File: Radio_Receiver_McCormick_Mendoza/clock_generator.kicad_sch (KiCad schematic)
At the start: 32 parts, among them J10 CLK_2, J11 I_LO, J12 Q_LO, J24 CLK_0, J9 CLK_1, U5 Si5351A-B-GT, U6 SN74AC74DR, Y1 ASTX-H11-24.576MHZ-T

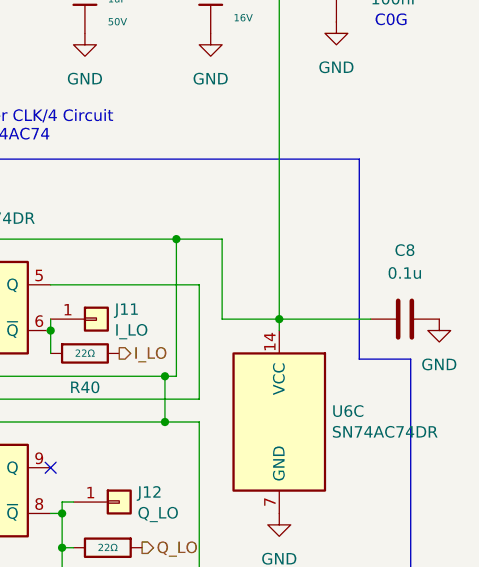
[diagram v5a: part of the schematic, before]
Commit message: Created low mono, high stereo impedance DAC audio outlets
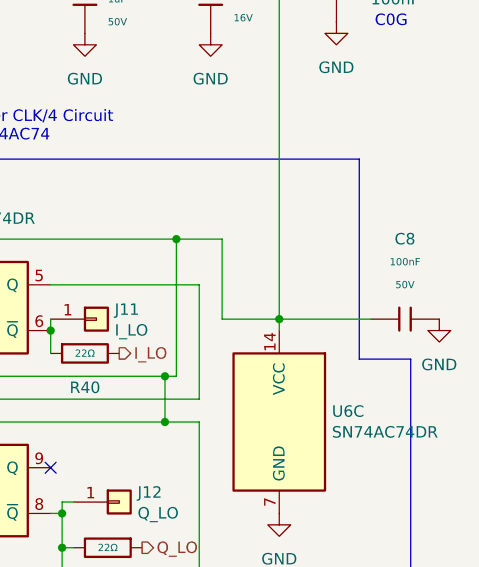
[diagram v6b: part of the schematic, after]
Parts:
- removed C8: 0.1u, Capacitor_THT:C_Disc_D5.1mm_W3.2mm_P5.00mm, symbol Device:C
- added C8: 100nF, PCM_JLCPCB:C_0402, symbol PCM_JLCPCB-Capacitors:0402,100nF,(2)
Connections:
- net GND: now also C8.2
- net at C71.1, C72.1, FB13.2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: now also C8.1
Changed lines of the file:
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@@
+	)
+	(symbol
+		(lib_id "PCM_JLCPCB-Capacitors:0402,100nF,(2)")
+		(at 207.01 82.55 90)
+		(unit 1)
+		(body_style 1)
+		(exclude_from_sim no)
+		(in_bom yes)
+		(on_board yes)
+		(in_pos_files yes)
+		(dnp no)
+		(fields_autoplaced yes)
+		(property "Reference" "C8"
+			(at 207.01 73.66 90)
+			(show_name no)
+			(do_not_autoplace no)
+			(effects
+				(font
+					(size 1.27 1.27)
+				)
+			)
+		)
+		(property "Value" "100nF"
+			(at 207.01 76.2 90)
+			(show_name no)
+			(do_not_autoplace no)
+			(effects
+				(font
+					(size 0.8 0.8)
+				)
+			)
+		)
+		(property "Footprint" "PCM_JLCPCB:C_0402"
+			(at 207.01 84.328 90)
+			(hide yes)
+			(show_name no)
+			(do_not_autoplace no)
+			(effects
+				(font
+					(size 1.27 1.27)
+				)
+			)
+		)
+		(property "Datasheet" "https://www.lcsc.com/datasheet/lcsc_datasheet_2304140030_Samsung-Electro-Mechanics-CL05B104KB54PNC_C307331.pdf"
+			(at 207.01 82.55 0)
+			(hide yes)
+			(show_name no)
+			(do_not_autoplace no)
+			(effects
+				(font
+					(size 1.27 1.27)
+				)
+			)
+		)
+		(property "Description" "50V 100nF X7R ±10% 0402 Multilayer Ceramic Capacitors MLCC - SMD/SMT ROHS"
+			(at 207.01 82.55 0)
+			(hide yes)
+			(show_name no)
+			(do_not_autoplace no)
+			(effects
+				(font
+					(size 1.27 1.27)
+				)
+			)
+		)
+		(property "LCSC" "C307331"
+			(at 207.01 82.55 0)
+			(hide yes)
+			(show_name no)
+			(do_not_autoplace no)
+			(effects
+				(font
+					(size 1.27 1.27)
+				)
+			)
+		)
+		(property "Stock" "8389599"
+			(at 207.01 82.55 0)
+			(hide yes)
+			(show_name no)
+			(do_not_autoplace no)
+			(effects
+				(font
+					(size 1.27 1.27)
+				)
+			)
+		)
+		(property "Price" "0.008USD"
+			(at 207.01 82.55 0)
+			(hide yes)
+			(show_name no)
+			(do_not_autoplace no)
+			(effects
+				(font
+					(size 1.27 1.27)
+				)
+			)
+		)
+		(property "Process" "SMT"
+			(at 207.01 82.55 0)
+			(hide yes)
+			(show_name no)
+			(do_not_autoplace no)
+			(effects
+				(font
+					(size 1.27 1.27)
+				)
+			)
+		)
+		(property "Minimum Qty" "20"
+			(at 207.01 82.55 0)
+			(hide yes)
+			(show_name no)
+			(do_not_autoplace no)
+			(effects
+				(font
+					(size 1.27 1.27)
+				)
+			)
+		)
+		(property "Attrition Qty" "10"
+			(at 207.01 82.55 0)
+			(hide yes)
+			(show_name no)
+			(do_not_autoplace no)
+			(effects
+				(font
+					(size 1.27 1.27)
+				)
+			)
+		)
+		(property "Class" "Basic Component"
+			(at 207.01 82.55 0)
+			(hide yes)
+			(show_name no)
+			(do_not_autoplace no)
+			(effects
+				(font
+					(size 1.27 1.27)
+				)
+			)
+		)
+		(property "Category" "Capacitors,Multilayer Ceramic Capacitors MLCC - SMD/SMT"
+			(at 207.01 82.55 0)
+			(hide yes)
+			(show_name no)
+			(do_not_autoplace no)
+			(effects
+				(font
+					(size 1.27 1.27)
+				)
+			)
+		)
+		(property "Manufacturer" "Samsung Electro-Mechanics"
+			(at 207.01 82.55 0)
+			(hide yes)
+			(show_name no)
+			(do_not_autoplace no)
+			(effects
+				(font
+					(size 1.27 1.27)
+				)
+			)
+		)
+		(property "Part" "CL05B104KB54PNC"
+			(at 207.01 82.55 0)
+			(hide yes)
+			(show_name no)
+			(do_not_autoplace no)
+			(effects
+				(font
+					(size 1.27 1.27)
+				)
+			)
+		)
+		(property "Voltage Rated" "50V"
+			(at 207.01 78.74 90)
+			(show_name no)
+			(do_not_autoplace no)
+			(effects
+				(font
+					(size 0.8 0.8)
+				)
+			)
+		)
+		(property "Tolerance" "±10%"
+			(at 207.01 82.55 0)
+			(hide yes)
+			(show_name no)
+			(do_not_autoplace no)
+			(effects
+				(font
+					(size 1.27 1.27)
+				)
+			)
+		)
+		(property "Capacitance" "100nF"
+			(at 207.01 82.55 0)
+			(hide yes)
+			(show_name no)
+			(do_not_autoplace no)
+			(effects
+				(font
+					(size 1.27 1.27)
+				)
+			)
+		)
+		(property "Temperature Coefficient" "X7R"
+			(at 207.01 82.55 0)
+			(hide yes)
+			(show_name no)
+			(do_not_autoplace no)
+			(effects
+				(font
+					(size 1.27 1.27)
+				)
+			)
+		)
+		(pin "2"
+		)
+		(pin "1"
+		)
+		(instances
+			(project "Radio_Receiver_McCormick_Mendoza"
+				(path "/f31d31ab-6846-4f3a-92b1-aa5a6a13373f/f64ea8ac-f7b3-4ac7-b675-bede152c9b4e"
+					(reference "C8")
+					(unit 1)
+				)
+			)
+		)
 	)
 	(symbol
@@
 					(unit 1)
 				)
-			)
-		)
-	)
-	(symbol
-		(lib_id "Device:C")
-		(at 207.01 82.55 90)
-		(unit 1)
-		(body_style 1)
-		(exclude_from_sim no)
-		(in_bom yes)
-		(on_board yes)
-		(in_pos_files yes)
-		(dnp no)
-		(fields_autoplaced yes)
-		(property "Reference" "C8"
-			(at 207.01 74.93 90)
-			(show_name no)
-			(do_not_autoplace no)
-			(effects
-				(font
-					(size 1.27 1.27)
-				)
-			)
-		)
-		(property "Value" "0.1u"
-			(at 207.01 77.47 90)
-			(show_name no)
-			(do_not_autoplace no)
-			(effects
-				(font
-					(size 1.27 1.27)
-				)
-			)
-		)
-		(property "Footprint" "Capacitor_THT:C_Disc_D5.1mm_W3.2mm_P5.00mm"
-			(at 210.82 81.5848 0)
-			(hide yes)
-			(show_name no)
-			(do_not_autoplace no)
-			(effects
-				(font
-					(size 1.27 1.27)
-				)
-			)
-		)
-		(property "Datasheet" ""
-			(at 207.01 82.55 0)
-			(hide yes)
-			(show_name no)
-			(do_not_autoplace no)
-			(effects
-				(font
-					(size 1.27 1.27)
-				)
-			)
-		)
-		(property "Description" "Unpolarized capacitor"
-			(at 207.01 82.55 0)
-			(hide yes)
-			(show_name no)
-			(do_not_autoplace no)
-			(effects
-				(font
-					(size 1.27 1.27)
-				)
-			)
-		)
-		(pin "1"
-		)
-		(pin "2"
-		)
-		(instances
-			(project "Radio_Receiver_McCormick_Mendoza"
-				(path "/f31d31ab-6846-4f3a-92b1-aa5a6a13373f/f64ea8ac-f7b3-4ac7-b675-bede152c9b4e"
-					(reference "C8")
-					(unit 1)
-				)

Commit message: Added MicroSD card and verified footprints
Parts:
- C8: Manufacturer Samsung Electro-Mechanics -> (none)
- JP12: footprint (none) -> Jumper:SolderJumper-2_P1.3mm_Open_RoundedPad1.0x1.5mm
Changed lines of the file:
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@@
-			)
-		)
-		(property "Manufacturer" "Samsung Electro-Mechanics"
-			(at 207.01 82.55 0)
-			(hide yes)
-			(show_name no)
-			(do_not_autoplace no)
-			(effects
-				(font
-					(size 1.27 1.27)
-				)
 			)
 		)
@@
 			)
 		)
-		(property "Footprint" ""
+		(property "Footprint" "Jumper:SolderJumper-2_P1.3mm_Open_RoundedPad1.0x1.5mm"
 			(at 58.42 107.95 0)
 			(hide yes)

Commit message: Updated footprints
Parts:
- Y1: footprint ASTX-H11-24.576MHZ-T:XTAL_ASTX-H11-24.576MHZ-T -> ASTX_H11_24_576MHZ_T:XTAL_ASTX-H11-24.576MHZ-T
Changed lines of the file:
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@@
 			)
 		)
-		(property "Footprint" "ASTX-H11-24.576MHZ-T:XTAL_ASTX-H11-24.576MHZ-T"
+		(property "Footprint" "ASTX_H11_24_576MHZ_T:XTAL_ASTX-H11-24.576MHZ-T"
 			(at 43.18 86.36 0)
 			(hide yes)
